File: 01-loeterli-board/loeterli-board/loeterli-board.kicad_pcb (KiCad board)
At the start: 2 copper layers, 100 x 60 mm, 55 parts, among them J1 RPC1-12RB-6P, J3 Conn_01x04, J5 Screw_Terminal_01x03, Q1 PSMN5R2-60YL, SW1 SW_Push, SW2 SW_Push, SW3 SW_Push, SW4 SW_Push, U1 VOM1271T, U2 STM32F103C8Tx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

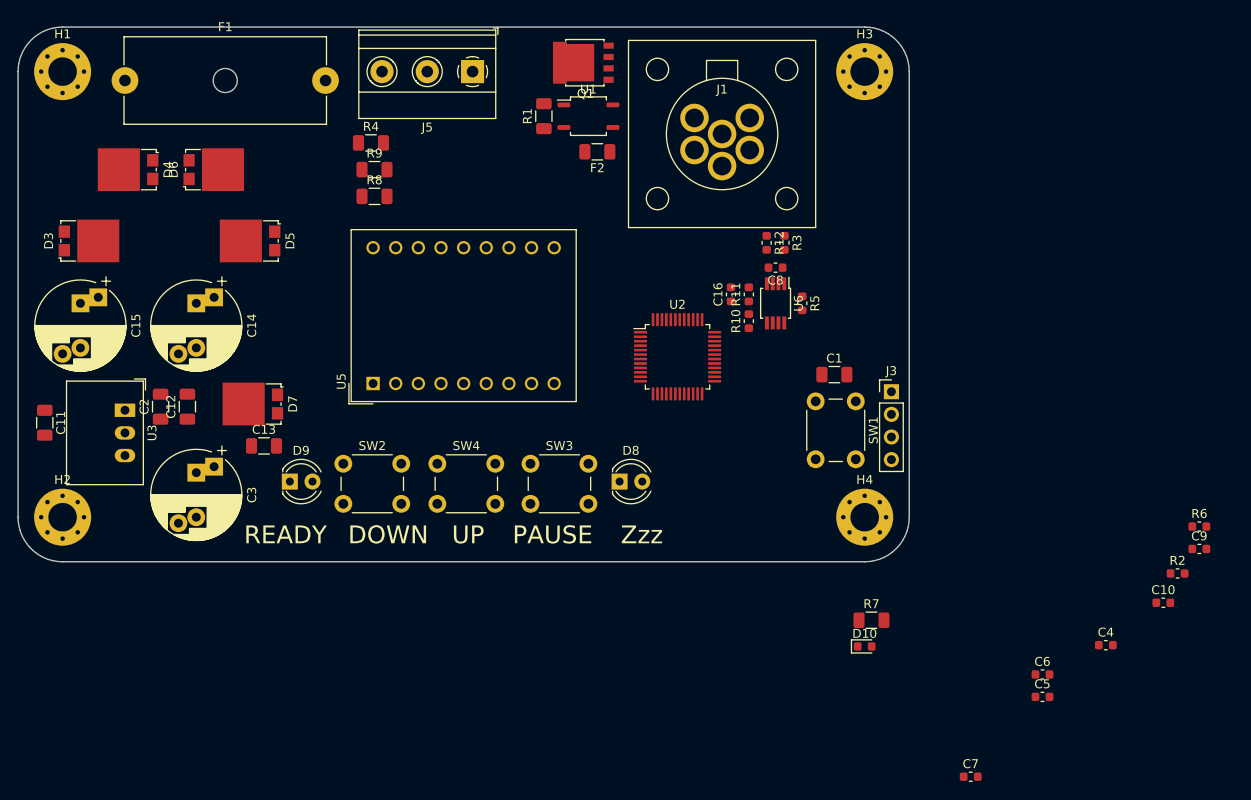
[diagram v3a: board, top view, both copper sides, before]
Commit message: logo + res for leds
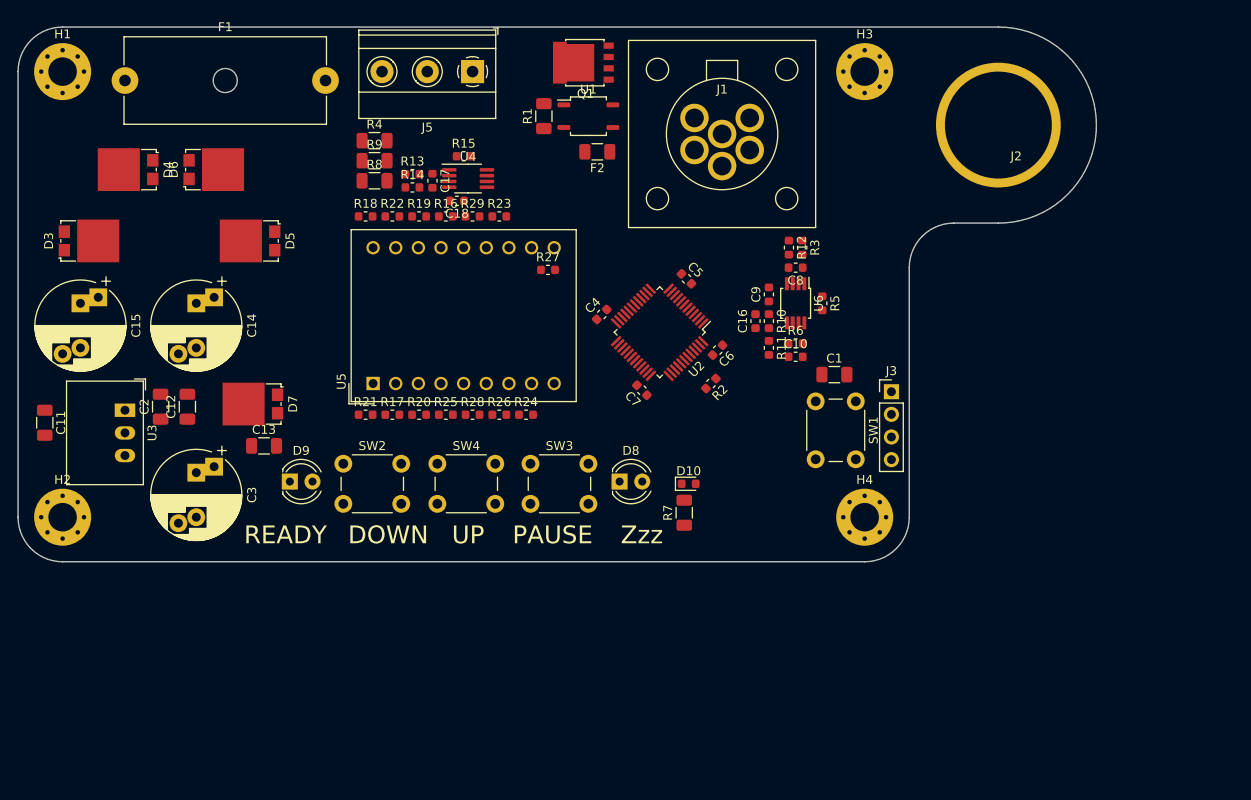
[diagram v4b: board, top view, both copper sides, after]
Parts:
- added C17: C, Capacitor_SMD:C_0603_1608Metric, F.Cu at (166.5, 67.2)
- added C18: C, Capacitor_SMD:C_0603_1608Metric, F.Cu at (169.2, 69.5)
- added J2: Conn_01x01, loeterli:handpiece-holder, F.Cu at (230.0, 61.0)
- added R13: 100R, Resistor_SMD:R_0603_1608Metric, F.Cu at (164.2, 66.5)
- added R14: 100R, Resistor_SMD:R_0603_1608Metric, F.Cu at (164.2, 68.0)
- added R15: 845R, Resistor_SMD:R_0603_1608Metric, F.Cu at (170.0, 64.5)
- added R16: 680R, Resistor_SMD:R_0603_1608Metric, F.Cu at (168.0, 71.2)
- added R17: 680R, Resistor_SMD:R_0603_1608Metric, F.Cu at (162.0, 93.5)
- added R18: 680R, Resistor_SMD:R_0603_1608Metric, F.Cu at (159.0, 71.2)
- added R19: 680R, Resistor_SMD:R_0603_1608Metric, F.Cu at (165.0, 71.2)
- added R20: 680R, Resistor_SMD:R_0603_1608Metric, F.Cu at (165.0, 93.5)
- added R21: 680R, Resistor_SMD:R_0603_1608Metric, F.Cu at (159.0, 93.5)
- added R22: 680R, Resistor_SMD:R_0603_1608Metric, F.Cu at (162.0, 71.2)
- added R23: 680R, Resistor_SMD:R_0603_1608Metric, F.Cu at (174.0, 71.2)
- added R24: 680R, Resistor_SMD:R_0603_1608Metric, F.Cu at (177.0, 93.5)
- added R25: 680R, Resistor_SMD:R_0603_1608Metric, F.Cu at (168.0, 93.5)
- added R26: 680R, Resistor_SMD:R_0603_1608Metric, F.Cu at (174.0, 93.5)
- added R27: 680R, Resistor_SMD:R_0603_1608Metric, F.Cu at (179.5, 77.2)
- added R28: 680R, Resistor_SMD:R_0603_1608Metric, F.Cu at (171.0, 93.5)
- added R29: 680R, Resistor_SMD:R_0603_1608Metric, F.Cu at (171.0, 71.2)
- added U4: AD8227, Package_SO:MSOP-8_3x3mm_P0.65mm, F.Cu at (170.5, 67.0)
- R12, R3: value 100 -> 100R
- R5: value 845 -> 845R
- SW2, SW3, SW4: footprint Button_Switch_THT:SW_PUSH_6mm_H4.3mm -> Button_Switch_THT:SW_PUSH_6mm_H7.3mm
- moved C4 67.6 mm to (185.5, 82.2), turned to 45 degrees
- moved C5 61.6 mm to (195.0, 78.2), turned to 315 degrees
- moved C7 56.9 mm to (190.0, 90.8), turned to 135 degrees
- moved R2 56.5 mm to (197.8, 90.0), turned to 225 degrees
- moved C9 56.1 mm to (204.2, 80.0), turned to 90 degrees
- moved C6 51.5 mm to (198.5, 86.2), turned to 225 degrees
- moved R6 49.7 mm to (207.2, 85.5)
- moved C10 49.6 mm to (207.2, 87.0)
- moved D10 26.9 mm to (195.2, 101.2)
- moved R7 24.2 mm to (194.8, 104.5), turned to 90 degrees
- moved R11 6.41 mm to (204.2, 86.0), turned to 270 degrees
- moved C16 4.07 mm to (202.8, 83.0)
- moved U2 3.40 mm to (192.0, 84.2), turned to 225 degrees
- moved R12 2.56 mm to (206.5, 74.8)
- moved C8 2.25 mm to (207.2, 77.0)
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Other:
- board size 100 x 60 mm -> 121 x 60 mm

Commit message: misc
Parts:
- moved R27 6.49 mm to (177.0, 71.2)
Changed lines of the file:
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@@
   )
   (module Resistor_SMD:R_0603_1608Metric (layer F.Cu)
-    (at 179.4625 77.25)
+    (at 177 71.25)
     (descr "Resistor SMD 0603 (1608 Metric), square (rectangular) end terminal, IPC_7351 nominal, (Body size source: http://www.tortai-tech.com/upload/download/2011102023233369053.pdf), generated with kicad-footprint-generator")
     (tags resistor)

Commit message: pinbelegung etc
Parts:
- added C19: C, Capacitor_SMD:C_1206_3216Metric, F.Cu at (235.7, 97.7)
- added C20: C, Capacitor_SMD:C_1206_3216Metric, F.Cu at (235.7, 101.0)
- added C21: C, Capacitor_SMD:C_1206_3216Metric, F.Cu at (241.3, 97.7)
- added C22: C, Capacitor_SMD:C_1206_3216Metric, F.Cu at (235.7, 104.3)
- added C23: C, Capacitor_SMD:C_1206_3216Metric, F.Cu at (241.3, 101.0)
- added C24: C, Capacitor_SMD:C_0603_1608Metric, F.Cu at (246.9, 104.4)
- added D1: SP0502BAHT, Package_TO_SOT_SMD:SOT-23, F.Cu at (246.3, 98.3)
- added R30: R, Resistor_SMD:R_0603_1608Metric, F.Cu at (254.6, 97.3)
- added R31: R, Resistor_SMD:R_0603_1608Metric, F.Cu at (242.9, 108.9)
- added R32: R, Resistor_SMD:R_0603_1608Metric, F.Cu at (250.5, 99.8)
- added R33: R, Resistor_SMD:R_0603_1608Metric, F.Cu at (242.9, 106.4)
- added R34: R, Resistor_SMD:R_0603_1608Metric, F.Cu at (250.5, 97.3)
- added R35: R, Resistor_SMD:R_0603_1608Metric, F.Cu at (246.1, 101.9)
- added R36: R, Resistor_SMD:R_0603_1608Metric, F.Cu at (238.9, 107.2)
- added R37: R, Resistor_SMD:R_0603_1608Metric, F.Cu at (240.5, 103.9)
- added R38: R, Resistor_SMD:R_0603_1608Metric, F.Cu at (234.9, 107.2)
- added R39: R, Resistor_SMD:R_0603_1608Metric, F.Cu at (254.6, 99.8)
- added R40: R, Resistor_SMD:R_0603_1608Metric, F.Cu at (246.9, 106.9)
- added R41: R, Resistor_SMD:R_0603_1608Metric, F.Cu at (250.9, 102.3)
- added R42: R, Resistor_SMD:R_0603_1608Metric, F.Cu at (250.9, 104.9)
- moved SW2 8.07 mm to (163.2, 103.5), turned to 180 degrees
- moved SW4 7.95 mm to (173.6, 103.5), turned to 180 degrees
- moved SW3 7.91 mm to (184.0, 103.5), turned to 180 degrees
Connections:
- D8 pad 1: Net-(D8-Pad1) -> LED_ZZZ
- D9 pad 1: Net-(D9-Pad1) -> LED_RDY
- J1 pad 6: Net-(J1-Pad6) -> SLEEP_EXT
- J2 pad 1: Net-(J2-Pad1) -> SLEEP_MOUNT
- J3 pad 1: Net-(J3-Pad1) -> +3V3
- J3 pad 2: Net-(J3-Pad2) -> SWDIO
- J3 pad 3: Net-(J3-Pad3) -> SWCLK
- J3 pad 4: Net-(J3-Pad4) -> GND
- R16 pad 1: Net-(R16-Pad1) -> DIG1_B
- R17 pad 1: Net-(R17-Pad1) -> DIG1_D
- R18 pad 1: Net-(R18-Pad1) -> DIG1_F
- R19 pad 1: Net-(R19-Pad1) -> DIG1_A
- R20 pad 1: Net-(R20-Pad1) -> DIG1_C
- R21 pad 1: Net-(R21-Pad1) -> DIG1_E
- R22 pad 1: Net-(R22-Pad1) -> DIG1_G
- R23 pad 1: Net-(R23-Pad1) -> DIG2_A
- R24 pad 1: Net-(R24-Pad1) -> DIG2_C
- R25 pad 1: Net-(R25-Pad1) -> DIG2_E
- R26 pad 1: Net-(R26-Pad1) -> DIG2_G
- R27 pad 1: Net-(R27-Pad1) -> DIG2_B
- R28 pad 1: Net-(R28-Pad1) -> DIG2_D
- R29 pad 1: Net-(R29-Pad1) -> DIG2_F
- SW2 pad 1: Net-(SW2-Pad1) -> GND
- SW3 pad 1: Net-(SW3-Pad1) -> GND
- SW4 pad 1: Net-(SW4-Pad1) -> GND
- U2 pad 10: Net-(U2-Pad10) -> TEMP
- U2 pad 11: Net-(U2-Pad11) -> V_RECT_SENSE
- U2 pad 12: Net-(U2-Pad12) -> I_SENSE
- U2 pad 13: Net-(U2-Pad13) -> nGATE
- U2 pad 15: Net-(U2-Pad15) -> DIG2_B
- U2 pad 16: Net-(U2-Pad16) -> DIG2_A
- U2 pad 17: Net-(U2-Pad17) -> DIG2_F
- U2 pad 18: Net-(U2-Pad18) -> DIG1_B
- U2 pad 19: Net-(U2-Pad19) -> DIG1_A
- U2 pad 21: Net-(U2-Pad21) -> DIG1_G
- U2 pad 22: Net-(U2-Pad22) -> DIG1_F
- U2 pad 25: Net-(U2-Pad25) -> DIG1_E
- U2 pad 26: Net-(U2-Pad26) -> DIG1_D
- U2 pad 27: Net-(U2-Pad27) -> DIG1_C
- U2 pad 28: Net-(U2-Pad28) -> DIG2_E
- U2 pad 29: Net-(U2-Pad29) -> DIG2_D
- U2 pad 30: Net-(U2-Pad30) -> DIG2_G
- U2 pad 31: Net-(U2-Pad31) -> DIG2_C
- U2 pad 32: Net-(U2-Pad32) -> LED_RDY
- U2 pad 33: Net-(U2-Pad33) -> SW_DOWN
- U2 pad 34: Net-(U2-Pad34) -> SWDIO
- U2 pad 37: Net-(U2-Pad37) -> SWCLK
- U2 pad 39: Net-(U2-Pad39) -> SW_UP
- U2 pad 40: Net-(U2-Pad40) -> SW_ZZZ
- U2 pad 41: Net-(U2-Pad41) -> LED_ZZZ
- U2 pad 42: Net-(U2-Pad42) -> ZCD
- U2 pad 45: Net-(U2-Pad45) -> SLEEP_EXT
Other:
- net class Default: clearance 0.2 -> 0.3; via_dia 0.8 -> 0.6; via_drill 0.4 -> 0.3
- rule trace_clearance: 0.2 -> 0.3

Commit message: layout
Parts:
- moved J2 2.92 mm to (227.5, 59.5)
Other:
- board size 121 x 60 mm -> 117 x 60 mm
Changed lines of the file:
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@@
-(kicad_pcb (version 20171130) (host pcbnew 5.1.4+dfsg1-1)
+(kicad_pcb (version 20171130) (host pcbnew 5.1.2)
   (general
     (thickness 1.6)
@@
   )
   (module loeterli:handpiece-holder (layer F.Cu)
-    (at 230 61)
+    (at 227.5 59.5)
     (fp_text reference J2 (at 2 3.5) (layer F.SilkS)
       (effects (font (size 1 1) (thickness 0.15)))
@@
     )
   )
-  (gr_line (start 230 72) (end 225 72) (layer Edge.Cuts) (width 0.05))
-  (gr_arc (start 225 77) (end 225 72) (angle -90) (layer Edge.Cuts) (width 0.05))
-  (gr_arc (start 230 61) (end 230 72) (angle -180) (layer Edge.Cuts) (width 0.05))
+  (gr_line (start 227.5 69) (end 225 69) (layer Edge.Cuts) (width 0.05))
+  (gr_arc (start 227.5 59.5) (end 227.5 69) (angle -180) (layer Edge.Cuts) (width 0.05))
+  (gr_arc (start 225 74) (end 225 69) (angle -90) (layer Edge.Cuts) (width 0.05))
+  (gr_arc (start 215 105) (end 215 110) (angle -90) (layer Edge.Cuts) (width 0.05))
+  (gr_arc (start 125 55) (end 125 50) (angle -90) (layer Edge.Cuts) (width 0.05))
+  (gr_arc (start 125 105) (end 120 105) (angle -90) (layer Edge.Cuts) (width 0.05))
+  (gr_line (start 220 74) (end 220 105) (layer Edge.Cuts) (width 0.05))
   (gr_text UP (at 170.499999 107) (layer F.SilkS)
     (effects (font (size 2 2) (thickness 0.3)))
@@
   )
   (gr_line (start 170 46) (end 170 157) (layer Eco1.User) (width 0.15))
-  (gr_arc (start 215 105) (end 215 110) (angle -90) (layer Edge.Cuts) (width 0.05))
-  (gr_arc (start 125 105) (end 120 105) (angle -90) (layer Edge.Cuts) (width 0.05))
-  (gr_arc (start 125 55) (end 125 50) (angle -90) (layer Edge.Cuts) (width 0.05))
-  (gr_line (start 230 50) (end 125 50) (layer Edge.Cuts) (width 0.05))
-  (gr_line (start 220 105) (end 220 77) (layer Edge.Cuts) (width 0.05))
+  (gr_line (start 227.5 50) (end 125 50) (layer Edge.Cuts) (width 0.05))
   (gr_line (start 125 110) (end 215 110) (layer Edge.Cuts) (width 0.05))
   (gr_line (start 120 55) (end 120 105) (layer Edge.Cuts) (width 0.05))

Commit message: layout changes
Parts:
- C19, C20, C21, C22, C23: footprint Capacitor_SMD:C_1206_3216Metric -> Capacitor_SMD:C_0603_1608Metric
- moved R34 91.7 mm to (158.8, 95.8), turned to 90 degrees
- moved R37 87.7 mm to (153.0, 97.3), turned to 180 degrees
- moved R42 84.5 mm to (175.4, 67.1), turned to 90 degrees
- moved R30 82.6 mm to (172.0, 95.9), turned to 270 degrees
- moved R31 81.9 mm to (162.0, 95.8), turned to 270 degrees
- moved C24 79.3 mm to (177.0, 67.1), turned to 270 degrees
- moved C20 75.4 mm to (160.4, 95.8), turned to 270 degrees
- moved R39 75.0 mm to (186.3, 68.8), turned to 180 degrees
- moved R33 74.8 mm to (168.8, 95.9), turned to 90 degrees
- moved R40 70.8 mm to (186.3, 70.4)
- moved R32 67.9 mm to (182.7, 95.9), turned to 270 degrees
- moved R35 66.9 mm to (179.5, 95.9), turned to 90 degrees
- moved C19 65.3 mm to (170.4, 95.9), turned to 270 degrees
- moved C21 60.2 mm to (181.1, 95.9), turned to 270 degrees
- moved C22 59.0 mm to (186.3, 72.0)
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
